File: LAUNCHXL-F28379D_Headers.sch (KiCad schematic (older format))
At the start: 8 parts, among them U1 AMP_DUE_SCH, U4 LoRa

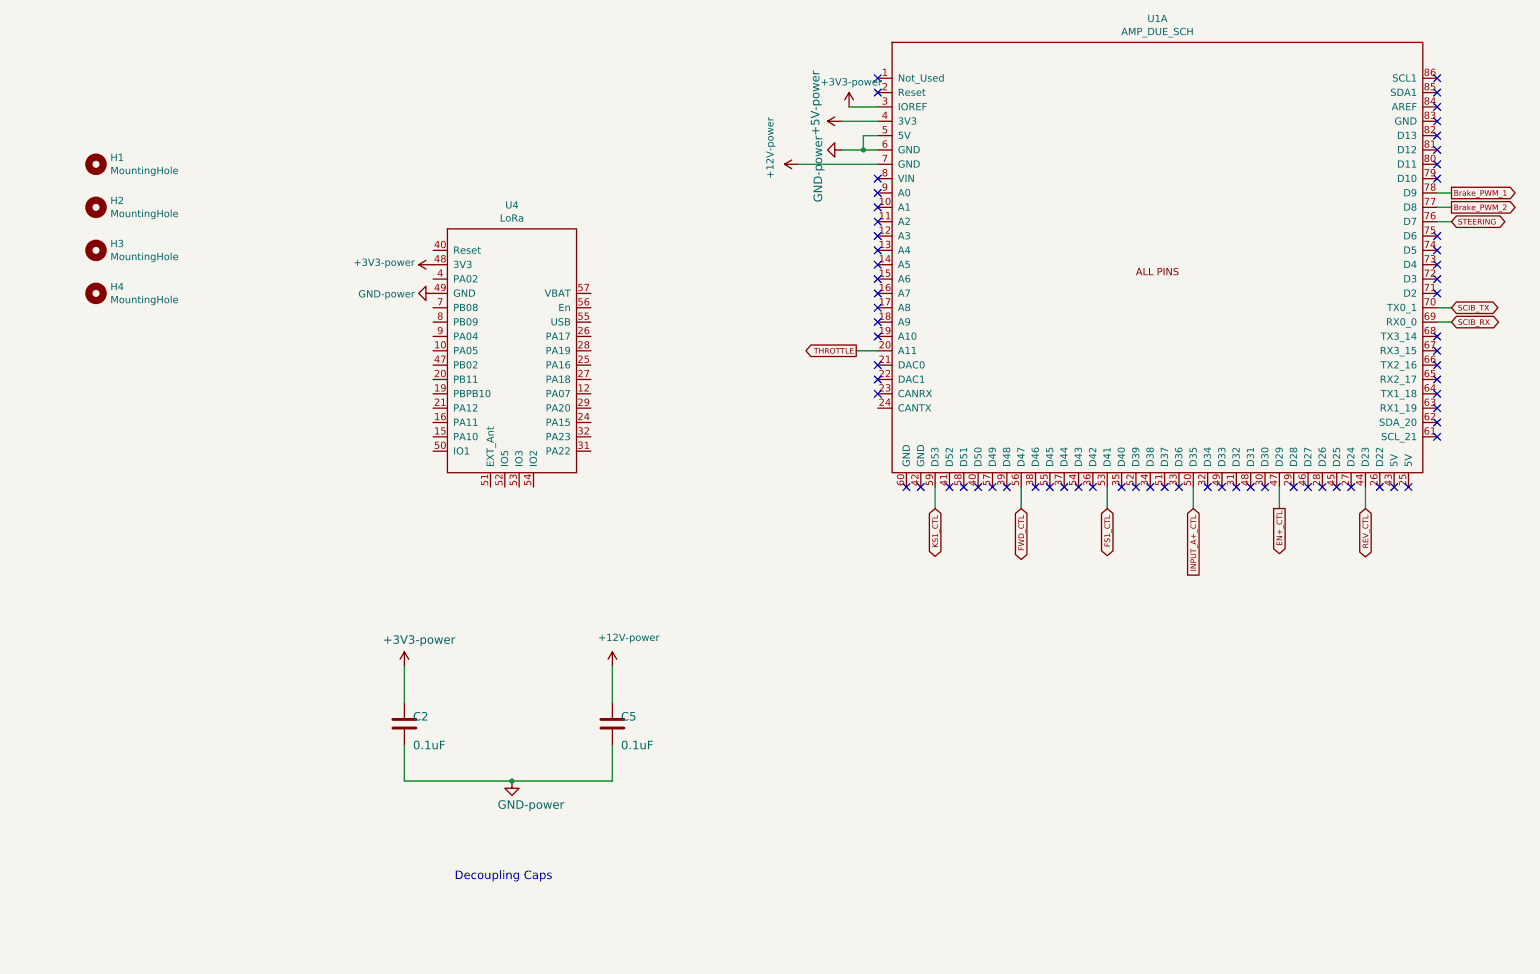
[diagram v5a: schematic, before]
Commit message: Added AND gate for Feather LoRa, and changed over to through hole components
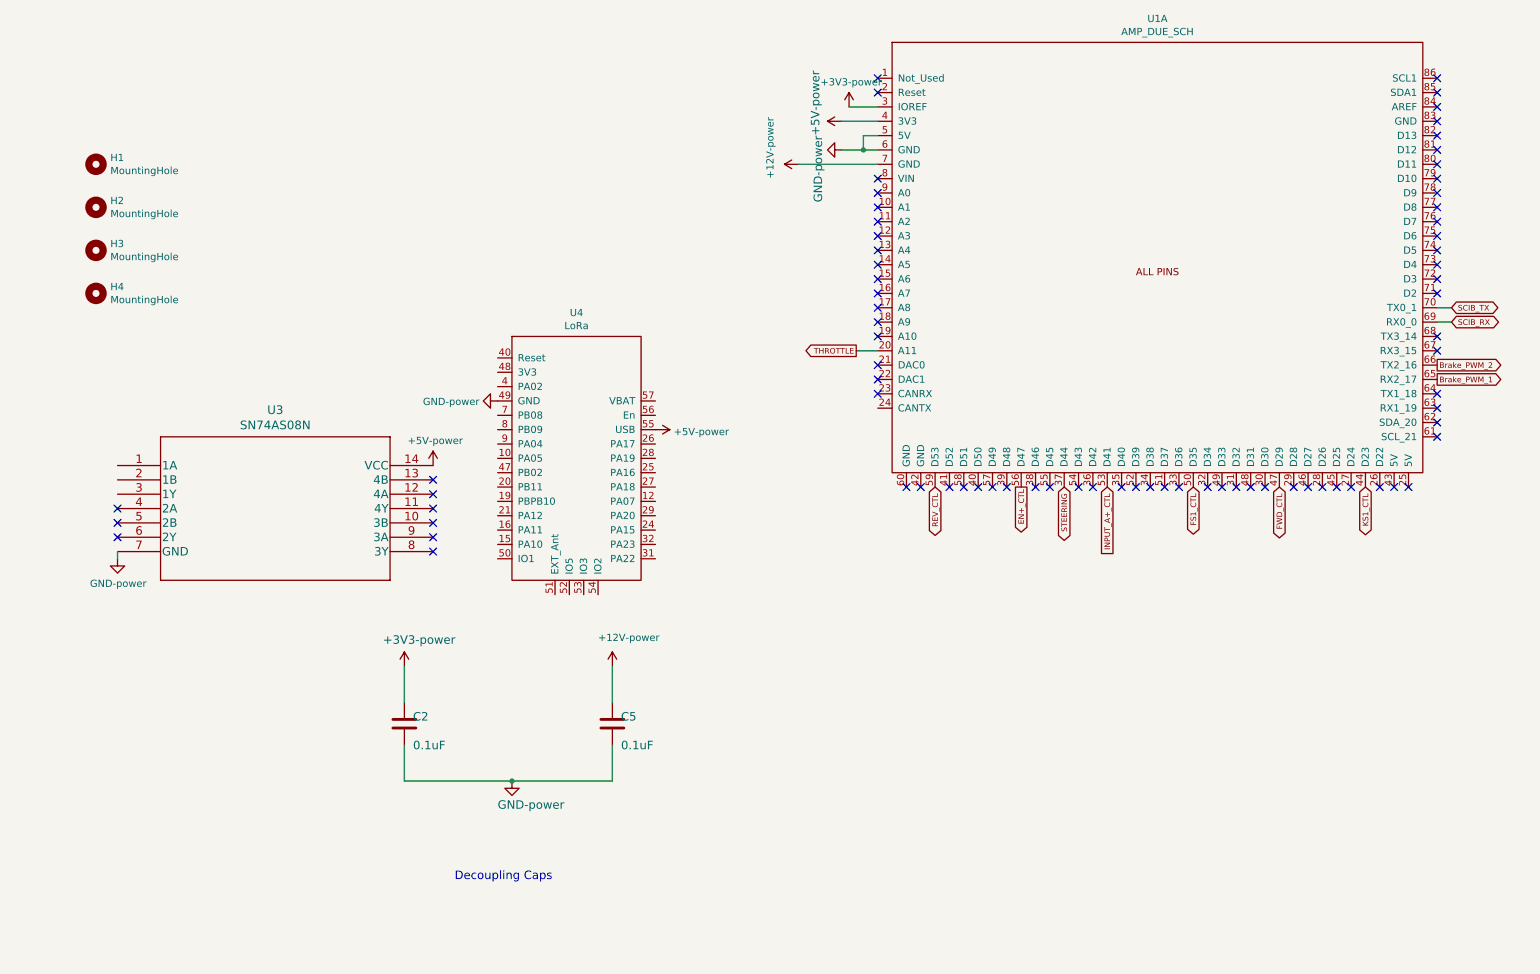
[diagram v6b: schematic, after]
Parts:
- added U3: SN74AS08N, Drivetrain_control:SN74AS08N, symbol 2021-01-12_19-55-02:SN74AS08N
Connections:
- net +3V3: no longer U4.48 (3V3)
- net +5V: now also U4.55 (USB), U3.14 (VCC)
- net Brake_PWM_1: now also U1.65 (RX2_17); no longer U1.78 (D9)
- net Brake_PWM_2: now also U1.66 (TX2_16); no longer U1.77 (D8)
- net EN+_CTL: now also U1.56 (D47); no longer U1.47 (D29)
- net FS1_CTL: now also U1.50 (D35); no longer U1.53 (D41)
- net FWD_CTL: now also U1.47 (D29); no longer U1.56 (D47)
- net GND: now also U3.7 (GND)
- net INPUT_A+_CTL: now also U1.53 (D41); no longer U1.50 (D35)
- net KS1_CTL: now also U1.44 (D23); no longer U1.59 (D53)
- net REV_CTL: now also U1.59 (D53); no longer U1.44 (D23)
- net STEERING: now also U1.37 (D44); no longer U1.76 (D7)
- no-connect marks 68 -> 77
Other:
- moved on the sheet: U4
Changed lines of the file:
@@
 Wire Wire Line
 	10500 3200 10600 3200
-Text GLabel 7000 4600 3    39   BiDi ~ 0
+Text GLabel 10000 4450 3    39   BiDi ~ 0
 KS1_CTL
 $Comp
@@
 	0    1    1    0
 $EndComp
-Wire Wire Line
-	10500 2600 10600 2600
-Wire Wire Line
-	10500 2500 10600 2500
-Wire Wire Line
-	10500 2400 10600 2400
 Text GLabel 6450 3500 0    39   Output ~ 0
 THROTTLE
-Text GLabel 10000 4600 3    39   BiDi ~ 0
+Text GLabel 7000 4450 3    39   BiDi ~ 0
 REV_CTL
-Text GLabel 7600 4600 3    39   BiDi ~ 0
+Text GLabel 9400 4450 3    39   BiDi ~ 0
 FWD_CTL
-Text GLabel 8200 4600 3    39   BiDi ~ 0
+Text GLabel 8800 4450 3    39   BiDi ~ 0
 FS1_CTL
-Text GLabel 8800 4600 3    39   Input ~ 0
+Text GLabel 8200 4450 3    39   Input ~ 0
 INPUT_A+_CTL
-Text GLabel 9400 4600 3    39   Output ~ 0
+Text GLabel 7600 4450 3    39   Output ~ 0
 EN+_CTL
-Text GLabel 10600 2600 2    39   BiDi ~ 0
+Text GLabel 7900 4450 3    39   BiDi ~ 0
 STEERING
-Text GLabel 10600 2500 2    39   Output ~ 0
+Text GLabel 10500 3600 2    39   Output ~ 0
 Brake_PWM_2
-Text GLabel 10600 2400 2    39   Output ~ 0
+Text GLabel 10500 3700 2    39   Output ~ 0
 Brake_PWM_1
 Text GLabel 10600 3200 2    39   BiDi ~ 0
@@
 Wire Wire Line
 	6450 3500 6600 3500
-Wire Wire Line
-	7000 4600 7000 4450
-Wire Wire Line
-	7600 4600 7600 4450
-Wire Wire Line
-	8200 4600 8200 4450
-Wire Wire Line
-	8800 4450 8800 4600
-Wire Wire Line
-	9400 4450 9400 4600
-Wire Wire Line
-	10000 4600 10000 4450
 Wire Wire Line
 	6350 1900 6600 1900
@@
 NoConn ~ 7700 4450
 NoConn ~ 7800 4450
-NoConn ~ 7900 4450
 NoConn ~ 8000 4450
 NoConn ~ 8100 4450
@@
 NoConn ~ 10500 3400
 NoConn ~ 10500 3500
-NoConn ~ 10500 3600
-NoConn ~ 10500 3700
-NoConn ~ 10500 3800
 NoConn ~ 10500 3900
 NoConn ~ 10500 4000
@@
 L PCB_2020-rescue:LoRa U4
 U 1 1 5FA8EB82
-P 4050 3550
-F 0 "U4" H 4050 4615 50  0000 C CNN
-F 1 "LoRa" H 4050 4524 50  0000 C CNN
-F 2 "Drivetrain_control:LoRa" H 4050 3950 50  0001 C CNN
-F 3 "" H 4050 3950 50  0001 C CNN
-	1    4050 3550
+P 4500 4300
+F 0 "U4" H 4500 5365 50  0000 C CNN
+F 1 "LoRa" H 4500 5274 50  0000 C CNN
+F 2 "Drivetrain_control:LoRa" H 4500 4700 50  0001 C CNN
+F 3 "" H 4500 4700 50  0001 C CNN
+	1    4500 4300
 	1    0    0    -1
 $EndComp
@@
 L PCB_2020-rescue:GND-power #PWR0109
 U 1 1 5FABAD06
-P 3500 3100
-F 0 "#PWR0109" H 3500 2850 50  0001 C CNN
-F 1 "GND-power" V 3505 2973 50  0000 R CNN
-F 2 "" H 3500 3100 50  0001 C CNN
-F 3 "" H 3500 3100 50  0001 C CNN
-	1    3500 3100
+P 3950 3850
+F 0 "#PWR0109" H 3950 3600 50  0001 C CNN
+F 1 "GND-power" V 3955 3723 50  0000 R CNN
+F 2 "" H 3950 3850 50  0001 C CNN
+F 3 "" H 3950 3850 50  0001 C CNN
+	1    3950 3850
 	0    1    1    0
 $EndComp
 $Comp
-L PCB_2020-rescue:+3V3-power #PWR0110
-U 1 1 5FABBDB9
-P 3500 2900
-F 0 "#PWR0110" H 3500 2750 50  0001 C CNN
-F 1 "+3V3-power" V 3515 3027 50  0000 L CNN
-F 2 "" H 3500 2900 50  0001 C CNN
-F 3 "" H 3500 2900 50  0001 C CNN
-	1    3500 2900
-	0    -1   -1   0
-$EndComp
+L PCB_2020-rescue:+5V-power #PWR0103
+U 1 1 5FECCC22
+P 5050 4050
+F 0 "#PWR0103" H 5050 3900 50  0001 C CNN
+F 1 "+5V-power" V 5065 4178 50  0000 L CNN
+F 2 "" H 5050 4050 50  0001 C CNN
+F 3 "" H 5050 4050 50  0001 C CNN
+	1    5050 4050
+	0    1    1    0
+$EndComp
+$Comp
+L 2021-01-12_19-55-02:SN74AS08N U3
+U 1 1 6002F62B
+P 1300 4300
+F 0 "U3" H 2400 4687 60  0000 C CNN
+F 1 "SN74AS08N" H 2400 4581 60  0000 C CNN
+F 2 "Drivetrain_control:SN74AS08N" H 2400 4540 60  0001 C CNN
+F 3 "" H 1300 4300 60  0000 C CNN
+	1    1300 4300
+	1    0    0    -1
+$EndComp
+NoConn ~ 3500 4400
+NoConn ~ 3500 4500
+NoConn ~ 3500 4600
+NoConn ~ 3500 4700
+NoConn ~ 3500 4800
+NoConn ~ 3500 4900
+NoConn ~ 1300 4800
+NoConn ~ 1300 4700
+NoConn ~ 1300 4600
+$Comp
+L PCB_2020-rescue:+5V-power #PWR0104
+U 1 1 6003277D
+P 3500 4300
+F 0 "#PWR0104" H 3500 4150 50  0001 C CNN
+F 1 "+5V-power" H 3515 4473 50  0000 C CNN
+F 2 "" H 3500 4300 50  0001 C CNN
+F 3 "" H 3500 4300 50  0001 C CNN
+	1    3500 4300
+	1    0    0    -1
+$EndComp
+$Comp
+L PCB_2020-rescue:GND-power #PWR0106
+U 1 1 6003369A
+P 1300 4950
+F 0 "#PWR0106" H 1300 4700 50  0001 C CNN
+F 1 "GND-power" H 1305 4777 50  0000 C CNN
+F 2 "" H 1300 4950 50  0001 C CNN
+F 3 "" H 1300 4950 50  0001 C CNN
+	1    1300 4950
+	1    0    0    -1
+$EndComp
+Wire Wire Line
+	1300 4900 1300 4950
+NoConn ~ 10500 2600
+NoConn ~ 10500 3800
+NoConn ~ 10500 2400
+NoConn ~ 10500 2500
 $EndSCHEMATC

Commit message: updated PCB with bluetooth connector for arduino signals
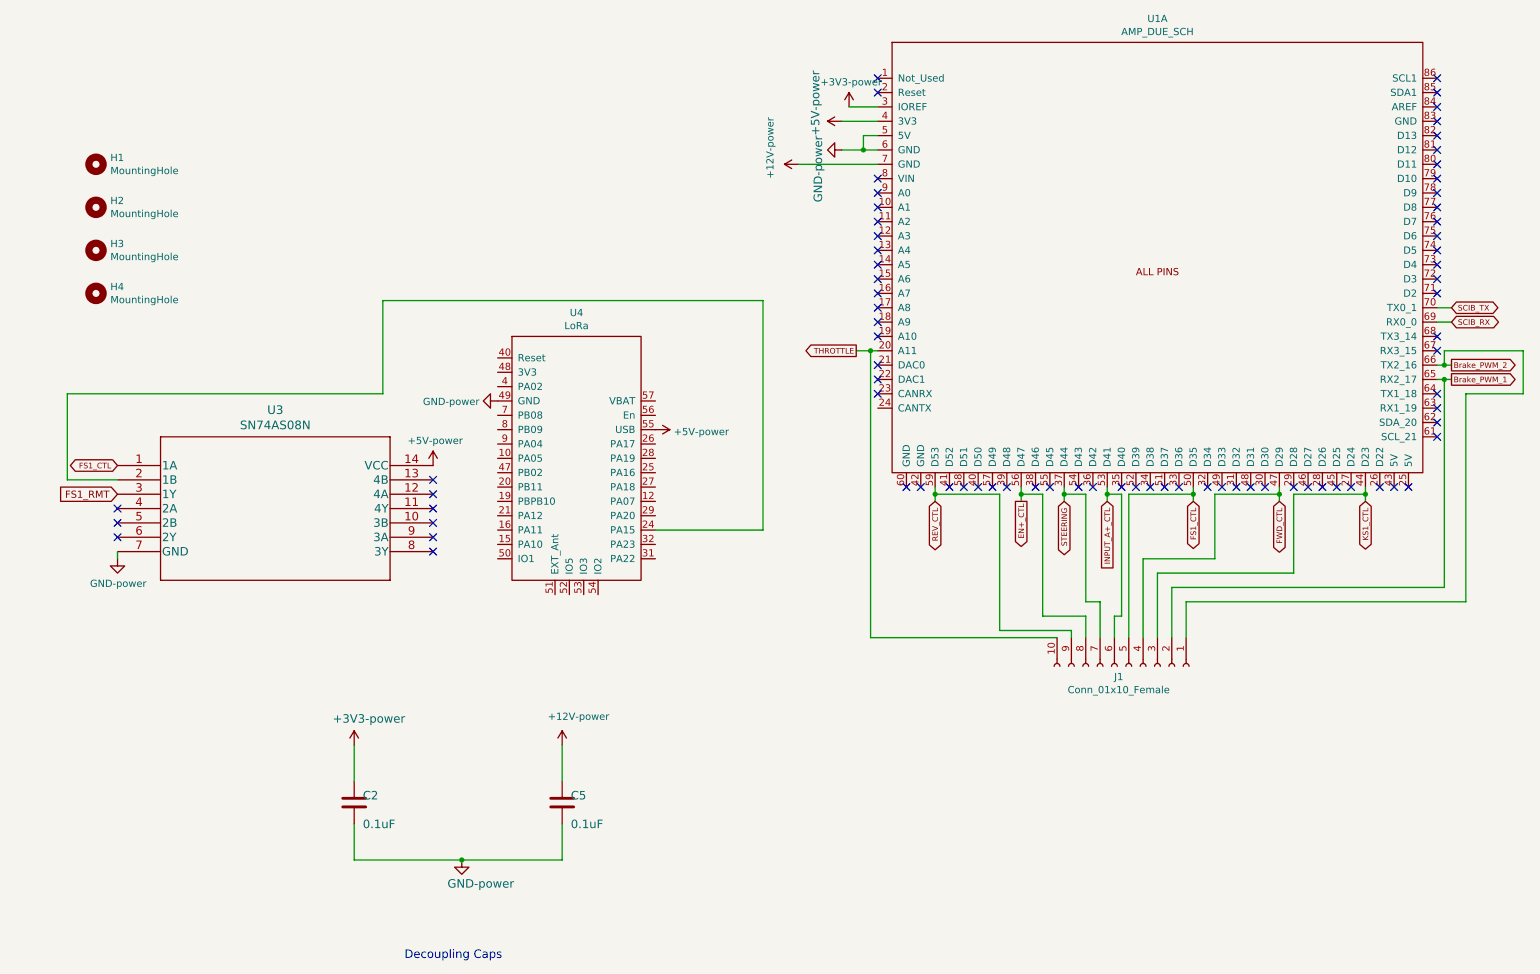
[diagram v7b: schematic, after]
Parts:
- added J1: Conn_01x10_Female, Connector_Molex:Molex_Mini-Fit_Jr_5566-10A2_2x05_P4.20mm_Vertical, symbol Connector:Conn_01x10_Female
- C2, C5: footprint Capacitor_THT:C_Disc_D3.0mm_W1.6mm_P2.50mm -> Capacitor_THT:CP_Radial_D4.0mm_P1.50mm
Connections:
- net Brake_PWM_1: now also J1.2 (Pin_2)
- net Brake_PWM_2: now also J1.1 (Pin_1)
- net EN+_CTL: now also J1.8 (Pin_8)
- net FS1_CTL: now also U3.1 (1A), J1.5 (Pin_5)
- net FWD_CTL: now also J1.4 (Pin_4)
- net INPUT_A+_CTL: now also J1.6 (Pin_6)
- net KS1_CTL: now also J1.3 (Pin_3)
- net REV_CTL: now also J1.9 (Pin_9)
- net STEERING: now also J1.7 (Pin_7)
- net THROTTLE: now also J1.10 (Pin_10)
- net at U4.24 (PA15): now also U3.2 (1B)
- net FS1_RMT: now reaches U3.3 (1Y)
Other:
- moved on the sheet: C2, C5
